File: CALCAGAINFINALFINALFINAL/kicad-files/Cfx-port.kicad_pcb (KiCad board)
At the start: 4 copper layers, 65 x 135.9 mm, 85 parts, among them J2 USB_C_Receptacle_USB2.0_16P, J3 Micro_SD_Card, J4 Conn_01x02, SW100 SW_SPST, SW101 SW_SPST, SW102 SW_SPST, SW49 SW_SPST, SW52 SW_SPST, SW55 SW_SPST, SW56 SW_SPST, SW57 SW_SPST, SW58 SW_SPST, SW59 SW_SPST, SW60 SW_SPST, SW61 SW_SPST, SW62 SW_SPST, SW63 SW_SPST, SW64 SW_SPST, SW65 SW_SPST, SW66 SW_SPST, SW67 SW_SPST, SW68 SW_SPST, SW69 SW_SPST, SW70 SW_SPST, SW71 SW_SPST, SW72 SW_SPST, SW73 SW_SPST, SW74 SW_SPST, SW75 SW_SPST, SW76 SW_SPST, SW77 SW_SPST, SW78 SW_SPST, SW79 SW_SPST, SW80 SW_SPST, SW81 SW_SPST, SW82 SW_SPST, SW83 SW_SPST, SW84 SW_SPST, SW85 SW_SPST, SW86 SW_SPST, SW87 SW_SPST, SW88 SW_SPST, SW89 SW_SPST, SW90 SW_SPST, SW91 SW_SPST, SW92 SW_SPST, SW93 SW_SPST, SW94 SW_SPST, SW95 SW_SPST, SW96 SW_SPST, SW97 SW_SPST, SW98 SW_SPST, SW99 SW_SPST, U5 TP4056-42-ESOP8, U6 TLV61070ADBV, U7 TCA9535DBR, U8 ESP32-S3-WROOM-2

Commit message: moment of truth lads im ordering the parts
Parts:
- added R5: 10k, Resistor_SMD:R_0201_0603Metric_Pad0.64x0.40mm_HandSolder, B.Cu at (146.1, 58.0)
- added R5: 10k, Resistor_SMD:R_0201_0603Metric_Pad0.64x0.40mm_HandSolder, B.Cu at (143.2, 58.0)
- ? (x2), R1, R10, R11, R12, R13, R14, R2, R3, R8, R9: footprint Resistor_SMD:R_0201_0603Metric -> Resistor_SMD:R_0201_0603Metric_Pad0.64x0.40mm_HandSolder
- B1, B2: renamed from REF**; value SW_Push_1P1T_NO_CK_KMR2 -> SW_Push_SPST_NO_Alps_SKRK; footprint Button_Switch_SMD:SW_Push_1P1T_NO_CK_KMR2 -> Button_Switch_SMD:SW_Push_SPST_NO_Alps_SKRK
- J3: footprint Connector_Card:microSD_HC_Molex_47219-2001 -> Connector_Card:microSD_HC_Wuerth_693072010801
- R4: renamed from REF**; value R_0603_1608Metric -> 10k
- moved C2 24.6 mm to (110.9, 57.5), turned to -90 degrees
- moved C1 24.4 mm to (112.5, 57.5), turned to -90 degrees
- moved B1 1.06 mm to (134.9, 27.9), turned to 180 degrees
- moved B2 0.78 mm to (150.7, 61.9), turned to -90 degrees
- moved D15 0.70 mm to (146.3, 86.2)
- moved D15 0.67 mm to (146.3, 87.3)
- moved REF** 0.64 mm to (129.2, 43.5)
- renumbered REF** to S1
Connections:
- U7 pad 11: unconnected-(U7-P07-Pad11) -> GND
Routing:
- net GND: track 101.9 -> 90.2 mm, vias 22 -> 25
- net /Keypad Matrix/C5: track 135.2 -> 143.8 mm
- net OV_D0: track 46.3 -> 39.0 mm
- net en: track 14.7 -> 8.44 mm
- net SCL: track 48.6 -> 53.1 mm, vias 3 -> 6
- net OV_HREF: track 22.6 -> 23.9 mm, vias 2 -> 1
- net VCC: track 25.0 -> 26.1 mm
- net SDA: track 53.1 -> 54.1 mm, vias 3 -> 5
- net 3V3: track 242.3 -> 241.6 mm
- net Net-(D20-A): track 0.93 -> 1.63 mm
- net OV_D3: track 28.8 -> 29.4 mm
- net /Keypad Matrix/C3: track 144.2 -> 143.6 mm
- net /Keypad Matrix/R2: track 153.0 -> 153.5 mm
- net OV_D2: track 38.4 -> 38.8 mm, vias 1 -> 2

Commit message: Turns out my whole power thing was absolutely retarded i should REALLY stop relying on gemini its actually retarded as fuh. Ima start js rawdogging it w forums and reddit. once its functional ima order it. i gota remember there no deadline better do it right the first time.
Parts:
- removed ?: 10k, Resistor_SMD:R_0201_0603Metric_Pad0.64x0.40mm_HandSolder
- added C66: C_0201_0603Metric, Capacitor_SMD:C_0201_0603Metric, B.Cu at (137.6, 105.0)
- added C672: C_0201_0603Metric, Capacitor_SMD:C_0201_0603Metric, B.Cu at (132.0, 103.0)
- added D1: D_0201_0603Metric, Diode_SMD:D_0201_0603Metric, B.Cu at (153.7, 127.6)
- added D2: D_0201_0603Metric, Diode_SMD:D_0201_0603Metric, B.Cu at (141.7, 127.6)
- added D3: D_0201_0603Metric, Diode_SMD:D_0201_0603Metric, B.Cu at (123.8, 88.6)
- added D4: D_0201_0603Metric, Diode_SMD:D_0201_0603Metric, B.Cu at (135.8, 79.5)
- added D5: D_0201_0603Metric, Diode_SMD:D_0201_0603Metric, B.Cu at (117.5, 77.2)
- added D6: D_0201_0603Metric, Diode_SMD:D_0201_0603Metric, B.Cu at (128.1, 77.2)
- added R67: 10k, Resistor_SMD:R_0603_1608Metric, B.Cu at (110.4, 35.0)
- added R67: 100, Resistor_SMD:R_0603_1608Metric, B.Cu at (112.3, 35.0)
- added SOt-23: idk, Package_TO_SOT_SMD:SOT-23, B.Cu at (110.3, 38.6)
- added r67: 22, Resistor_SMD:R_0603_1608Metric, B.Cu at (106.5, 35.4)
- J3: footprint Connector_Card:microSD_HC_Wuerth_693072010801 -> ButtonPads:CONN_47219-2001_MOL
- L2: value L -> 10
- R1, R3: value R -> 10k; footprint Resistor_SMD:R_0201_0603Metric_Pad0.64x0.40mm_HandSolder -> Resistor_SMD:R_0603_1608Metric
- R10, R11: value R -> 1k; footprint Resistor_SMD:R_0201_0603Metric_Pad0.64x0.40mm_HandSolder -> Resistor_SMD:R_0603_1608Metric
- R12, R13, R14, R2, R5 (x2), R8, R9: footprint Resistor_SMD:R_0201_0603Metric_Pad0.64x0.40mm_HandSolder -> Resistor_SMD:R_0603_1608Metric
- R123, R55: renamed from REF**; footprint Resistor_SMD:R_01005_0402Metric -> Resistor_SMD:R_0201_0603Metric
- R223: renamed from ?; footprint Resistor_SMD:R_0201_0603Metric_Pad0.64x0.40mm_HandSolder -> Resistor_SMD:R_0603_1608Metric
- moved C1 13.1 mm to (101.3, 64.2), turned to 180 degrees
- moved C2 10.6 mm to (101.2, 62.0), turned to 180 degrees
- moved R2 7.09 mm to (133.1, 36.9)
- moved R3 6.25 mm to (131.4, 30.3), turned to 90 degrees
- moved B1 4.31 mm to (139.2, 28.2), turned to 0 degrees
- moved L2 3.84 mm to (137.6, 98.9)
- moved R1 2.79 mm to (133.2, 33.6), turned to -90 degrees
- moved R14 2.30 mm to (130.4, 101.7)
- moved R13 1.85 mm to (130.5, 105.5)
- moved C6 1.70 mm to (130.4, 98.6)
- moved R9 1.41 mm to (151.4, 85.7)
- moved R8 1.28 mm to (152.3, 81.5)
- moved R5 0.70 mm to (143.9, 58.0)
- moved R12 0.67 mm to (133.3, 87.3)
- moved D15 0.67 mm to (146.6, 85.6)
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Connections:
- S1 pad 10: /esp32-s3 pinout/SCK -> /esp32-s3 pinout/DC
- S1 pad 11: 3V3 -> /esp32-s3 pinout/SCK
- S1 pad 17: GND -> (no net)
- S1 pad 18: GND -> (no net)
- S1 pad 19: GND -> (no net)
- S1 pad 20: GND -> (no net)
- S1 pad 21: GND -> (no net)
- S1 pad 22: GND -> (no net)
- S1 pad 23: GND -> (no net)
- S1 pad 24: GND -> (no net)
- S1 pad 25: GND -> (no net)
- S1 pad 26: GND -> (no net)
- S1 pad 27: GND -> (no net)
- S1 pad 28: GND -> (no net)
- S1 pad 29: GND -> (no net)
- S1 pad 30: GND -> (no net)
- S1 pad 31: GND -> (no net)
- S1 pad 32: GND -> (no net)
- S1 pad 33: (no net) -> 2v8
- S1 pad 34: GND -> cathode
- S1 pad 35: GND -> cathode
- S1 pad 36: GND -> cathode
- S1 pad 4: /esp32-s3 pinout/DC -> (no net)
- S1 pad 40: 3V3 -> GND
- S1 pad 5: (no net) -> GND
- S1 pad 7: (no net) -> 3V3
- U8 pad 26: unconnected-(U8-IO45-Pad26) -> (no net)
- U8 pad 35: (no net) -> BL
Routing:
- net BL: track 0.00 -> 42.4 mm, vias 0 -> 3
- net GND: track 90.2 -> 101.7 mm, vias 25 -> 28
- net /esp32-s3 pinout/CS1: track 31.9 -> 39.5 mm, vias 2 -> 3
- net /esp32-s3 pinout/CMD: track 31.6 -> 39.1 mm
- net cathode: track 0.00 -> 7.43 mm
- net 2v8: track 0.00 -> 7.18 mm, vias 0 -> 2
- net 3V3: track 241.6 -> 247.7 mm, vias 8 -> 6
- net /esp32-s3 pinout/SCK: track 61.9 -> 66.7 mm, vias 2 -> 4
- net Net-(U6-SW): track 6.72 -> 3.21 mm
- net Net-(U6-V_{FB}): track 3.55 -> 6.79 mm
- net /power-ic/BAT+: track 65.4 -> 62.3 mm
- net /esp32-s3 pinout/DC: track 48.9 -> 51.6 mm, vias 0 -> 2
- net /Keypad Matrix/R1: track 95.4 -> 97.0 mm, vias 7 -> 11
- net /Keypad Matrix/R4: track 142.9 -> 144.1 mm
- net OV_D7: track 32.0 -> 30.9 mm
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
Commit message: dude ima run one last check then tmw ima fr place the order foreal this time ong this is it twin
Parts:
- removed C66, C672: C_0201_0603Metric, Capacitor_SMD:C_0201_0603Metric
- removed L2: 10, Inductor_SMD:L_0603_1608Metric
- removed R13: 100k, Resistor_SMD:R_0603_1608Metric
- removed R14: 560k, Resistor_SMD:R_0603_1608Metric
- removed R223, R4: 10k, Resistor_SMD:R_0603_1608Metric
- removed U6: TLV61070ADBV, Package_TO_SOT_SMD:SOT-23-6
- added C6: 1µF, Capacitor_SMD:C_0603_1608Metric, B.Cu at (140.3, 101.7)
- added LDO: IC_TPS73733DCQR, ButtonPads:IC_TPS73733DCQR, B.Cu at (133.4, 102.2)
- added cuba: 100k, Resistor_SMD:R_0603_1608Metric, B.Cu at (142.9, 101.4)
- added r21: 100k, Resistor_SMD:R_0603_1608Metric, B.Cu at (142.9, 97.1)
- C6: value 22µF -> 1µF
- R123, R55: footprint Resistor_SMD:R_0201_0603Metric -> Resistor_SMD:R_0603_1608Metric
- R67: value 100 -> 1k
- moved R5 20.8 mm to (132.3, 42.9), turned to 0 degrees
- moved C5 16.7 mm to (141.4, 81.7), turned to -90 degrees
- moved C4 8.93 mm to (135.9, 81.6), turned to -90 degrees
- moved C6 7.30 mm to (137.6, 97.4)
- moved R55 3.27 mm to (135.4, 29.3), turned to 180 degrees
- moved B1 2.62 mm to (141.2, 29.9)
- moved R67 2.00 mm to (110.3, 34.9)
- moved R67 2.00 mm to (112.4, 35.0)
- moved J4 1.77 mm to (143.3, 107.7)
- moved R123 0.36 mm to (151.1, 54.5), turned to -90 degrees
- moved D4 0.32 mm to (135.9, 79.2)
- moved R2 0.32 mm to (133.2, 36.6)
- moved SW65 0.30 mm to (114.1, 102.3)
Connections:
- B1 pad 1: 3V3 -> boot
- R123 pad 1: 3V3 -> en
- R5 pad 1: SDA -> 3V3
- U8 pad 24: batprog -> SDA
- U8 pad 7: SDA -> batprog
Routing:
- net SDA: track 54.1 -> 42.5 mm, vias 5 -> 3
- net /power-ic/BAT+: track 62.3 -> 73.6 mm
- net GND: track 101.7 -> 91.2 mm
- net /Keypad Matrix/C5: track 143.8 -> 136.6 mm
- net 3V3: track 247.7 -> 254.8 mm
- net Net-(U6-V_{FB}): track 6.79 -> 0.00 mm
- net boot: track 1.75 -> 7.95 mm
- net batprog: track 60.2 -> 56.7 mm, vias 3 -> 4
- net Net-(U6-SW): track 3.21 -> 0.00 mm
- net /esp32-s3 pinout/MISO: track 20.5 -> 22.1 mm, vias 0 -> 2
- net OV_HREF: track 23.9 -> 24.8 mm
- net /Keypad Matrix/C3: track 143.4 -> 142.8 mm

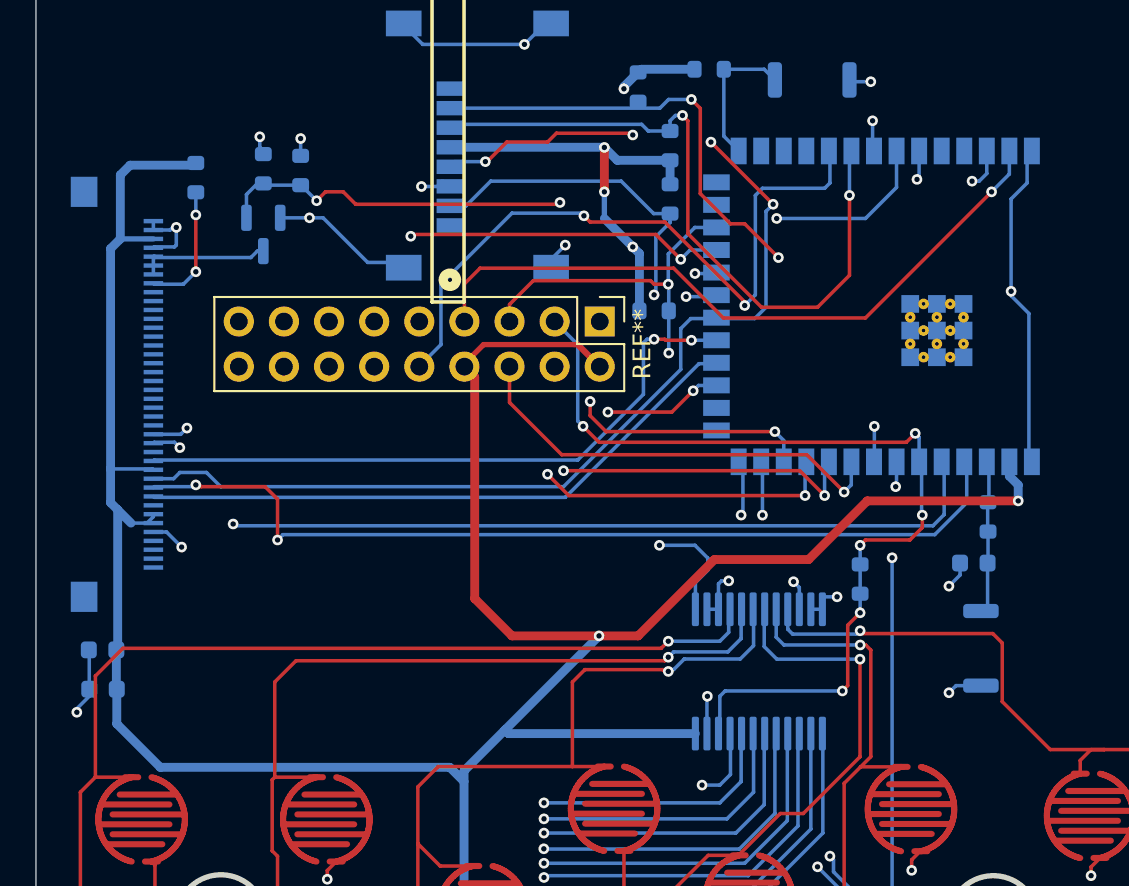
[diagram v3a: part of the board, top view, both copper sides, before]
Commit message: workin on matching up the pcb with the schematic gona chuck it on pcbreview then wait till i can stack up enough cash to order the first pcba. i need to make sure the design is 100% otherwise im js spending 300 bucks on a paperweight. so far the logic seems good js need to fix up some clerical errors w schematic.
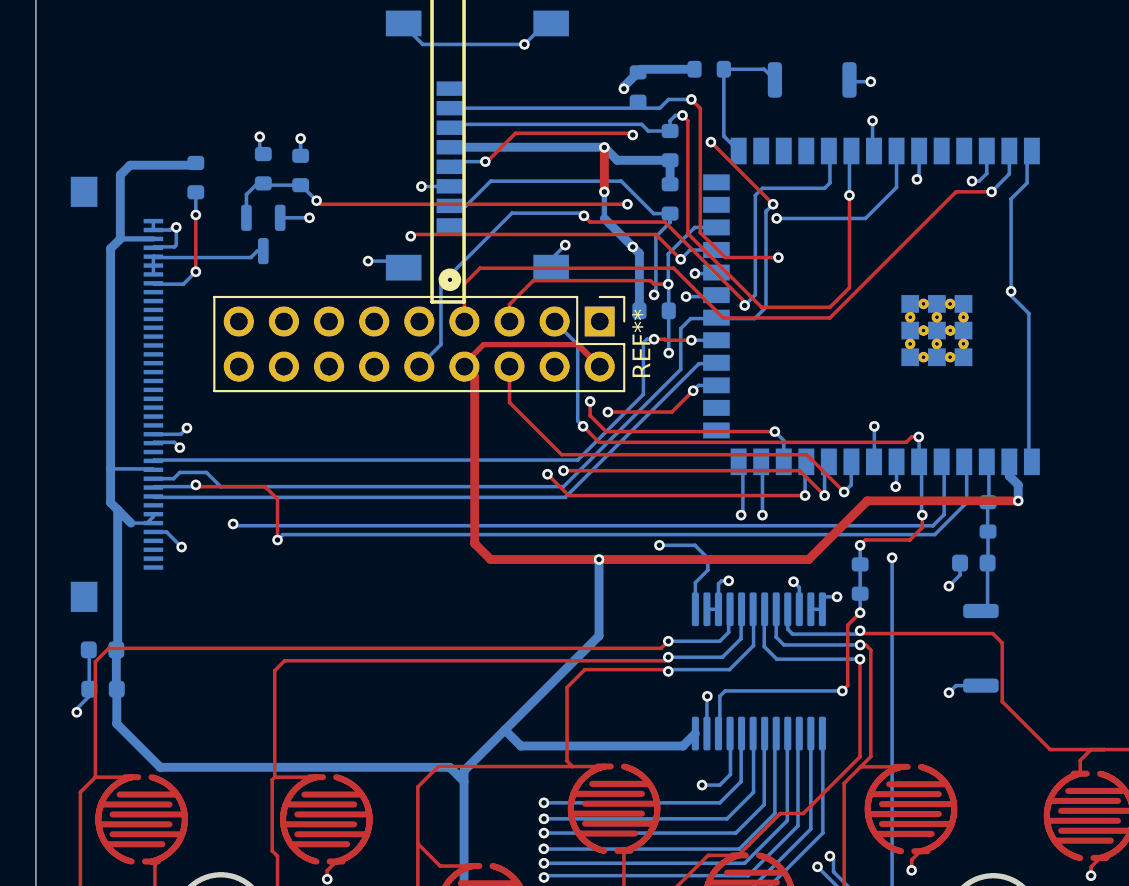
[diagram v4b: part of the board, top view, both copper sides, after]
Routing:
- net 3V3: track 254.8 -> 250.0 mm
- net GND: track 91.2 -> 87.4 mm, vias 28 -> 29
- net /esp32-s3 pinout/CS1: track 39.5 -> 40.8 mm

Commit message: yo chat this actually for reals the order now im ordering it and neva openin kicad again ong
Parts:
- removed C4: 10µF, Capacitor_SMD:C_0603_1608Metric
- removed D2, D4, D5: D_0201_0603Metric, Diode_SMD:D_0201_0603Metric
- removed SW102: SW_SPST, ButtonPads:conductive pad
- removed r67: 22, Resistor_SMD:R_0603_1608Metric
- added C6: 1µF, Capacitor_SMD:C_0603_1608Metric, B.Cu at (129.5, 98.7)
- added D8: 1N5819, Diode_SMD:Nexperia_CFP3_SOD-123W, B.Cu at (142.2, 96.3)
- added NIGERC: 100k, Resistor_SMD:R_0603_1608Metric, B.Cu at (140.4, 103.7)
- added Q1: DMP3099L, Package_TO_SOT_SMD:SOT-23, B.Cu at (138.7, 99.8)
- added R902: 10k, Resistor_SMD:R_0603_1608Metric, B.Cu at (132.3, 33.1)
- added U1: TPS73125DBV, Package_TO_SOT_SMD:SOT-23-5, B.Cu at (102.3, 69.1)
- added r2123: 4.7k, Resistor_SMD:R_0603_1608Metric, B.Cu at (133.2, 51.2)
- added toes1: 10uf, Capacitor_SMD:C_0603_1608Metric_Pad1.08x0.95mm_HandSolder, B.Cu at (129.0, 41.6)
- added toes4: 10uf, Capacitor_SMD:C_0603_1608Metric_Pad1.08x0.95mm_HandSolder, B.Cu at (125.7, 48.8)
- J2: footprint Connector_USB:USB_C_Receptacle_GCT_USB4105-xx-A_16P_TopMnt_Horizontal -> ButtonPads:TENSILITY_54-00304
- J3: footprint ButtonPads:CONN_47219-2001_MOL -> ButtonPads:CONN_TF-01A_HRO
- R12: value 1.2 -> 1.6
- R5: value 10k -> 4.7k
- moved D1 73.6 mm to (103.3, 74.0)
- moved D6 55.0 mm to (106.2, 127.6)
- moved R9 30.3 mm to (153.3, 115.9), turned to -90 degrees
- moved J2 28.4 mm to (160.9, 112.7)
- moved R8 28.1 mm to (153.3, 109.6), turned to 90 degrees
- moved D3 17.8 mm to (106.0, 88.6)
- moved C6 14.0 mm to (123.6, 97.3)
- moved J4 14.0 mm to (130.4, 113.2), turned to 90 degrees
- moved C6 13.4 mm to (129.4, 93.9)
- moved LDO 10.8 mm to (122.6, 102.2)
- moved r21 9.43 mm to (142.2, 106.5), turned to 180 degrees
- moved cuba 6.38 mm to (145.5, 107.2)
- moved C5 2.50 mm to (138.9, 81.7)
- moved R67 2.24 mm to (109.3, 32.9), turned to 90 degrees
- moved R67 2.06 mm to (111.6, 33.1), turned to 90 degrees
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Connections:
- net /esp32-s3 pinout/MOSI renamed MOSI
- net cathode renamed /esp32-s3 pinout/cathode
- C1 pad 1: 3V3 -> 2V8
- C2 pad 1: 3V3 -> 2V8
- D1 pad 1: /Keypad Matrix/R6 -> /Keypad Matrix/R1
- D1 pad 2: /Keypad Matrix/R6 -> /Keypad Matrix/R1
- D6 pad 1: /Keypad Matrix/R1 -> /Keypad Matrix/R6
- D6 pad 2: /Keypad Matrix/R1 -> /Keypad Matrix/R6
- LDO pad 1: 3V3 -> pwr
- LDO pad 2: /power-ic/BAT+ -> 3V3
- LDO pad 4: 3V3 -> pwr
- LDO pad 5: 3V3 -> pwr
- R123 pad 2: en -> 3V3
- R67 pad 1: GND -> BL1
- S1 pad 1: (no net) -> unconnected-(S1-Pin_1-Pad1)
- S1 pad 12: 3V3 -> 2V8
- S1 pad 14: (no net) -> unconnected-(S1-Pin_14-Pad14)
- S1 pad 17: (no net) -> unconnected-(S1-Pin_17-Pad17)
- S1 pad 18: (no net) -> unconnected-(S1-Pin_18-Pad18)
- S1 pad 19: (no net) -> unconnected-(S1-Pin_19-Pad19)
- S1 pad 2: (no net) -> unconnected-(S1-Pin_2-Pad2)
- S1 pad 20: (no net) -> unconnected-(S1-Pin_20-Pad20)
- S1 pad 21: (no net) -> unconnected-(S1-Pin_21-Pad21)
- S1 pad 22: (no net) -> unconnected-(S1-Pin_22-Pad22)
- S1 pad 23: (no net) -> unconnected-(S1-Pin_23-Pad23)
- S1 pad 24: (no net) -> unconnected-(S1-Pin_24-Pad24)
- S1 pad 25: (no net) -> unconnected-(S1-Pin_25-Pad25)
- S1 pad 26: (no net) -> unconnected-(S1-Pin_26-Pad26)
- S1 pad 27: (no net) -> unconnected-(S1-Pin_27-Pad27)
- S1 pad 28: (no net) -> unconnected-(S1-Pin_28-Pad28)
- S1 pad 29: (no net) -> unconnected-(S1-Pin_29-Pad29)
- S1 pad 3: (no net) -> unconnected-(S1-Pin_3-Pad3)
- S1 pad 30: (no net) -> unconnected-(S1-Pin_30-Pad30)
- S1 pad 31: (no net) -> unconnected-(S1-Pin_31-Pad31)
- S1 pad 32: (no net) -> unconnected-(S1-Pin_32-Pad32)
- S1 pad 33: 2v8 -> 2V8
- S1 pad 38: 3V3 -> GND
- S1 pad 39: GND -> 2V8
- S1 pad 4: (no net) -> unconnected-(S1-Pin_4-Pad4)
- S1 pad 40: GND -> 2V8
- S1 pad 6: 3V3 -> 2V8
- S1 pad 7: 3V3 -> 2V8
- S1 pad 8: (no net) -> unconnected-(S1-Pin_8-Pad8)
- SOt-23 pad 1: BL -> BL1
- U5 pad 4: /power-ic/BAT+ -> VCC
- U7 pad 11: GND -> unconnected-(U7-P07-Pad11)
- U8 pad 15: (no net) -> unconnected-(U8-IO3-Pad15)
- U8 pad 26: (no net) -> unconnected-(U8-IO45-Pad26)
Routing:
- net VCC: track 27.0 -> 93.1 mm, vias 0 -> 2
- net 3V3: track 250.0 -> 196.6 mm, vias 6 -> 7
- net 2V8: track 0.00 -> 39.6 mm
- net usb_N: track 44.1 -> 82.0 mm, vias 2 -> 3
- net /Keypad Matrix/R1: track 96.8 -> 133.8 mm, vias 11 -> 10
- net usb_P: track 45.8 -> 80.0 mm, vias 2 -> 5
- net pwr: track 0.00 -> 31.9 mm
- net /Keypad Matrix/C6: track 89.4 -> 66.2 mm
- net GND: track 87.4 -> 65.9 mm, vias 29 -> 34
- net /Keypad Matrix/R5: track 165.2 -> 147.1 mm, vias 7 -> 6
- net OV_D7: track 30.9 -> 43.9 mm
- net /esp32-s3 pinout/SCK: track 67.1 -> 75.1 mm, vias 4 -> 5
- net 2v8: track 7.18 -> 0.00 mm, vias 2 -> 0
- net OV_PCLK: track 47.9 -> 41.2 mm
- net /Keypad Matrix/R2: track 153.5 -> 160.0 mm
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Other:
- board text added: "+ -"
- board text added: "d"
